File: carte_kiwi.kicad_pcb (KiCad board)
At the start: 2 copper layers, 50 x 50 mm, 40 parts, among them IC1 MCP2562, P1 CONN_01X05, P2 CONN_01X03, P3 CONN_01X05, P4 CONN_01X03, P5 Serial Wire, P6 CAN_conn, P7 CONN_01X03, P8 CONN_01X03, P9 CAN_conn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

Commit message: Mise à jour des libs (zener, led, switch)
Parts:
- D1, D2, D3: value ZENERsmall -> D_Zener_Small
- SW1: value SW_PUSH_SMALL_H -> SW_Push
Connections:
- U3 pad 10: (no net) -> Net-(U3-Pad10)
- U3 pad 11: (no net) -> Net-(U3-Pad11)
- U3 pad 25: (no net) -> Net-(U3-Pad25)
- U3 pad 28: (no net) -> Net-(U3-Pad28)
- U3 pad 9: (no net) -> Net-(U3-Pad9)
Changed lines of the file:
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@@
     (zones 0)
     (modules 40)
-    (nets 36)
+    (nets 41)
   )
   (page A4)
@@
   (net 34 "Net-(D4-Pad2)")
   (net 35 "Net-(D5-Pad2)")
+  (net 36 "Net-(U3-Pad9)")
+  (net 37 "Net-(U3-Pad10)")
+  (net 38 "Net-(U3-Pad11)")
+  (net 39 "Net-(U3-Pad25)")
+  (net 40 "Net-(U3-Pad28)")
   (net_class Default "Ceci est la Netclass par défaut"
     (clearance 0.2)
@@
     (uvia_dia 0.3)
     (uvia_drill 0.1)
+    (add_net "Net-(U3-Pad10)")
+    (add_net "Net-(U3-Pad11)")
+    (add_net "Net-(U3-Pad25)")
+    (add_net "Net-(U3-Pad28)")
+    (add_net "Net-(U3-Pad9)")
   )
   (net_class DRC ""
@@
       (effects (font (size 1 1) (thickness 0.15)))
     )
-    (fp_text value ZENERsmall (at 0 2.1) (layer F.Fab)
+    (fp_text value D_Zener_Small (at 0 2.1) (layer F.Fab)
       (effects (font (size 1 1) (thickness 0.15)))
     )
@@
       (effects (font (size 1 1) (thickness 0.15)))
     )
-    (fp_text value ZENERsmall (at 0 2.1) (layer F.Fab)
+    (fp_text value D_Zener_Small (at 0 2.1) (layer F.Fab)
       (effects (font (size 1 1) (thickness 0.15)))
     )
@@
       (effects (font (size 1 1) (thickness 0.15)))
     )
-    (fp_text value ZENERsmall (at 0 2.1 270) (layer F.Fab)
+    (fp_text value D_Zener_Small (at 0 2.1 270) (layer F.Fab)
       (effects (font (size 1 1) (thickness 0.15)))
     )
@@
       (effects (font (size 1 1) (thickness 0.15)))
     )
-    (fp_text value SW_PUSH_SMALL_H (at 0 3 90) (layer F.Fab)
+    (fp_text value SW_Push (at 0 3 90) (layer F.Fab)
       (effects (font (size 1 1) (thickness 0.15)))
     )
@@
     (pad 8 smd rect (at -4.25 2.8) (size 1.2 0.6) (layers F.Cu F.Paste F.Mask)
       (net 11 TIM2|Hall3))
-    (pad 9 smd rect (at -2.8 4.25 90) (size 1.2 0.6) (layers F.Cu F.Paste F.Mask))
-    (pad 10 smd rect (at -2 4.25 90) (size 1.2 0.6) (layers F.Cu F.Paste F.Mask))
-    (pad 11 smd rect (at -1.2 4.25 90) (size 1.2 0.6) (layers F.Cu F.Paste F.Mask))
+    (pad 9 smd rect (at -2.8 4.25 90) (size 1.2 0.6) (layers F.Cu F.Paste F.Mask)
+      (net 36 "Net-(U3-Pad9)"))
+    (pad 10 smd rect (at -2 4.25 90) (size 1.2 0.6) (layers F.Cu F.Paste F.Mask)
+      (net 37 "Net-(U3-Pad10)"))
+    (pad 11 smd rect (at -1.2 4.25 90) (size 1.2 0.6) (layers F.Cu F.Paste F.Mask)
+      (net 38 "Net-(U3-Pad11)"))
     (pad 12 smd rect (at -0.4 4.25 90) (size 1.2 0.6) (layers F.Cu F.Paste F.Mask)
       (net 21 TIM3|PWM1))
@@
     (pad 24 smd rect (at 4.25 -2.8) (size 1.2 0.6) (layers F.Cu F.Paste F.Mask)
       (net 18 SWCLK))
-    (pad 25 smd rect (at 2.8 -4.25 90) (size 1.2 0.6) (layers F.Cu F.Paste F.Mask))
+    (pad 25 smd rect (at 2.8 -4.25 90) (size 1.2 0.6) (layers F.Cu F.Paste F.Mask)
+      (net 39 "Net-(U3-Pad25)"))
     (pad 26 smd rect (at 2 -4.25 90) (size 1.2 0.6) (layers F.Cu F.Paste F.Mask)
       (net 20 USART2_TX/SWO))
     (pad 27 smd rect (at 1.2 -4.25 90) (size 1.2 0.6) (layers F.Cu F.Paste F.Mask)
       (net 28 USART2_RX))
-    (pad 28 smd rect (at 0.4 -4.25 90) (size 1.2 0.6) (layers F.Cu F.Paste F.Mask))
+    (pad 28 smd rect (at 0.4 -4.25 90) (size 1.2 0.6) (layers F.Cu F.Paste F.Mask)
+      (net 40 "Net-(U3-Pad28)"))
     (pad 29 smd rect (at -0.4 -4.25 90) (size 1.2 0.6) (layers F.Cu F.Paste F.Mask)
       (net 32 USART1_TX/SCL))

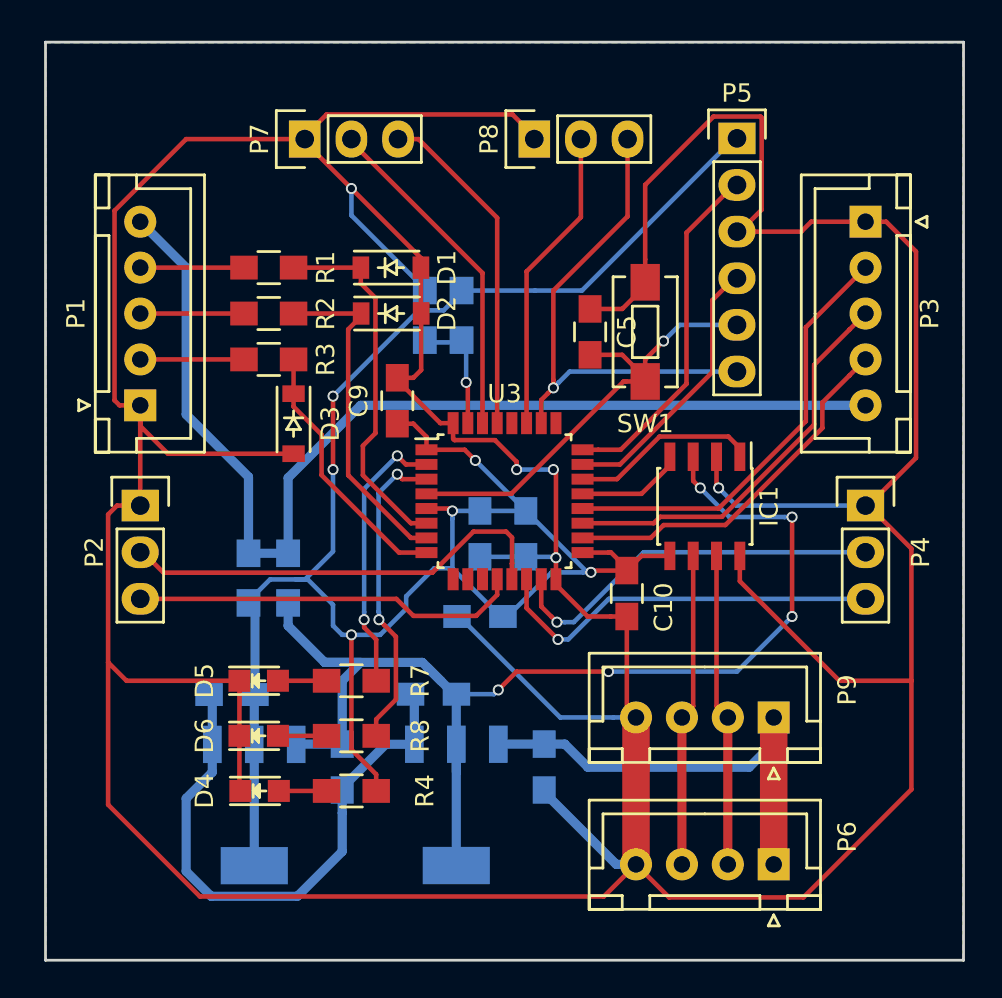
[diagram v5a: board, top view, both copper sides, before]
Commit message: retourné connecteur CAN
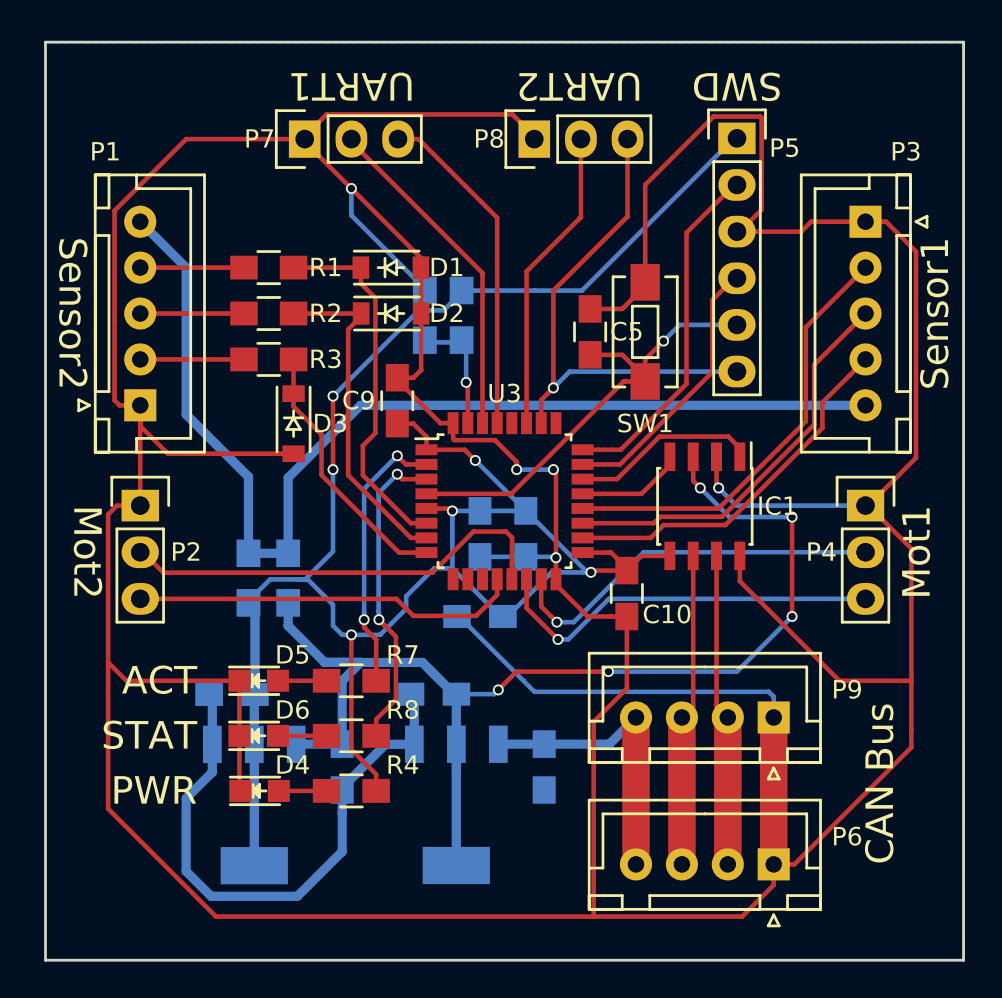
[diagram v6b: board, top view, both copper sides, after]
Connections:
- P6 pad 1: +9V -> GND
- P6 pad 4: GND -> +9V
- P9 pad 1: +9V -> GND
- P9 pad 4: GND -> +9V
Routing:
- net GND: track 337.7 -> 349.4 mm
- net +9V: track 25.5 -> 16.8 mm
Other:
- board text added: "ACT"
- board text added: "CAN Bus"
- board text added: "Mot1"
- board text added: "Mot2"
- board text added: "PWR"
- board text added: "STAT"
- board text added: "SWD"
- board text added: "Sensor1"
- board text added: "Sensor2"
- board text added: "UART1"
- board text added: "UART2"

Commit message: change de coté les capa de découplage et arrange un peu les choses
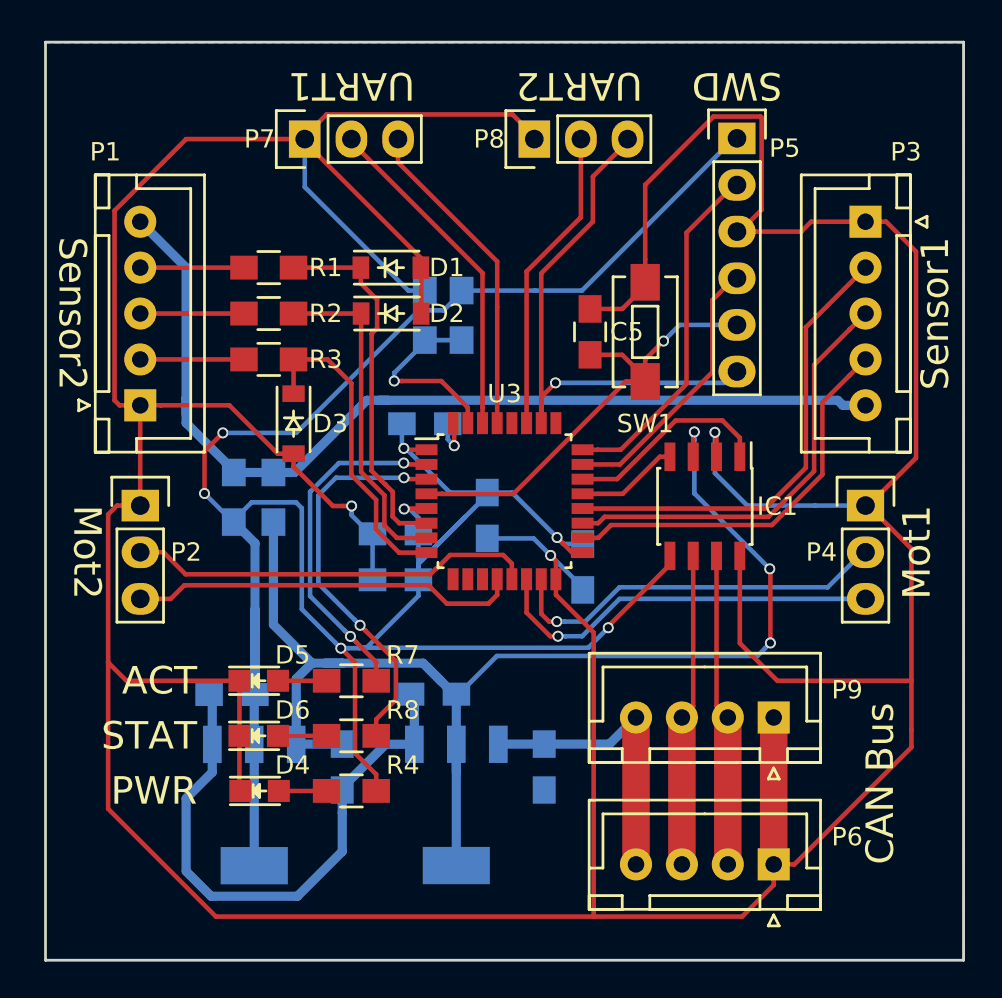
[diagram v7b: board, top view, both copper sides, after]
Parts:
- C10, C9: moved to B.Cu
- moved C7 7.53 mm to (144.4, 114.5), turned to 180 degrees
- moved C8 5.51 mm to (149.4, 111.0), turned to 270 degrees
- moved C6 4.60 mm to (144.4, 112.0), turned to 180 degrees
- moved R5 4.47 mm to (135.6, 110.0)
- moved R6 4.47 mm to (137.8, 110.0)
- moved C10 2.80 mm to (154.6, 113.8)
- moved C9 1.95 mm to (146.0, 106.0), turned to 0 degrees
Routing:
- net +3V3: track 118.2 -> 143.3 mm, vias 6 -> 7
- net GND: track 349.4 -> 328.4 mm, vias 5 -> 4
- net Sensor_PWR: track 59.8 -> 53.3 mm
- net STATUS_LED: track 17.2 -> 21.6 mm
- net +5V: track 66.2 -> 70.1 mm, vias 5 -> 3
- net ACTIVITY_LED: track 15.1 -> 18.8 mm
- net BOOT0: track 6.54 -> 10.3 mm
- net TIM2|Hall3: track 14.4 -> 17.3 mm
- net USART2_TX/SWO: track 27.8 -> 30.1 mm
- net TIM3|DIR1/PWM2: track 24.0 -> 22.2 mm
- net TIM1|Hall3: track 23.8 -> 25.3 mm
- net TIM1|ENCB/Hall2: track 22.0 -> 23.5 mm
- net TIM1|ENCA/Hall1: track 20.2 -> 21.7 mm
- net CAN_TX: track 10.3 -> 11.3 mm
- net USART1_TX/SCL: track 18.4 -> 17.7 mm

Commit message: ajoute les trou de vis et suprime les drawings de placement
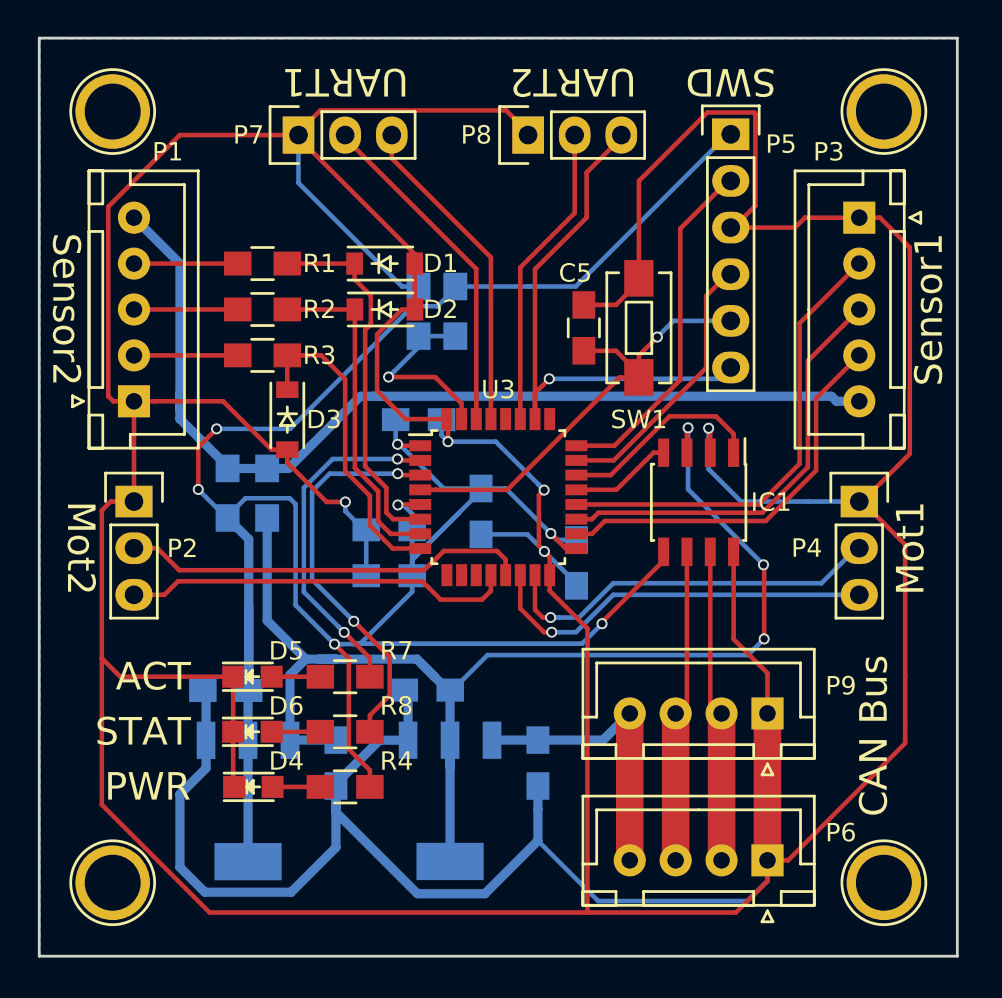
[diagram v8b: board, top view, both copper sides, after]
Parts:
- added REF**: 1pin, Connect:1pin, F.Cu at (171.0, 89.0)
- added REF**: 1pin, Connect:1pin, F.Cu at (129.0, 89.0)
- added REF**: 1pin, Connect:1pin, F.Cu at (129.0, 131.0)
- added REF**: 1pin, Connect:1pin, F.Cu at (171.0, 131.0)
- moved U2 0.40 mm to (136.4, 126.5)
- moved C1 0.40 mm to (152.2, 124.5)
- moved C10 0.40 mm to (154.3, 113.6)
- moved C2 0.40 mm to (146.1, 120.5)
- moved C3 0.40 mm to (141.2, 124.5)
- moved C4 0.40 mm to (135.2, 120.5)
- moved C5 0.40 mm to (154.7, 100.8)
- moved C6 0.40 mm to (144.1, 111.8)
- moved C7 0.40 mm to (144.1, 114.3)
- moved C8 0.40 mm to (149.1, 110.8)
- moved C9 0.40 mm to (145.7, 105.8)
- moved D1 0.40 mm to (143.8, 97.3)
- moved D2 0.40 mm to (143.8, 99.8)
- moved D3 0.40 mm to (138.5, 105.8)
- moved D4 0.40 mm to (136.7, 125.8)
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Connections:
- U3 pad 10: Net-(U3-Pad10) -> (no net)
- U3 pad 11: Net-(U3-Pad11) -> (no net)
- U3 pad 25: Net-(U3-Pad25) -> (no net)
- U3 pad 28: Net-(U3-Pad28) -> (no net)
- U3 pad 9: Net-(U3-Pad9) -> (no net)
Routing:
- net GND: track 328.4 -> 376.8 mm, vias 4 -> 5
